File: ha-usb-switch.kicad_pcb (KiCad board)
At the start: 2 copper layers, 30 x 55 mm, 9 parts, among them J1 USB4125-GF-A-0190_REVA2, J4 USB1046-XX-XXXX-X-B-X_REVB, Q2 AO3401A, Q3 AO3400A, SW2 SW_SPDT, U1 MOUDLE-SEEEDUINO-XIAO-ESP32C3

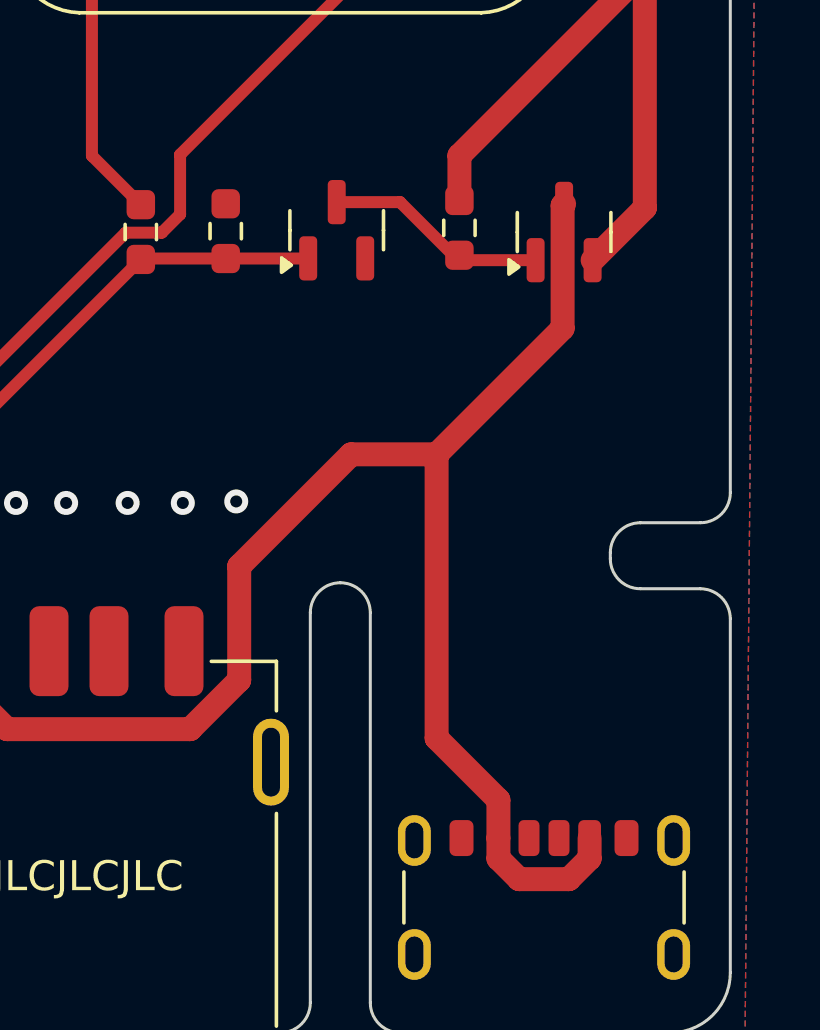
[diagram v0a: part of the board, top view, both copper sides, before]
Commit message: Add USB C sink pullups
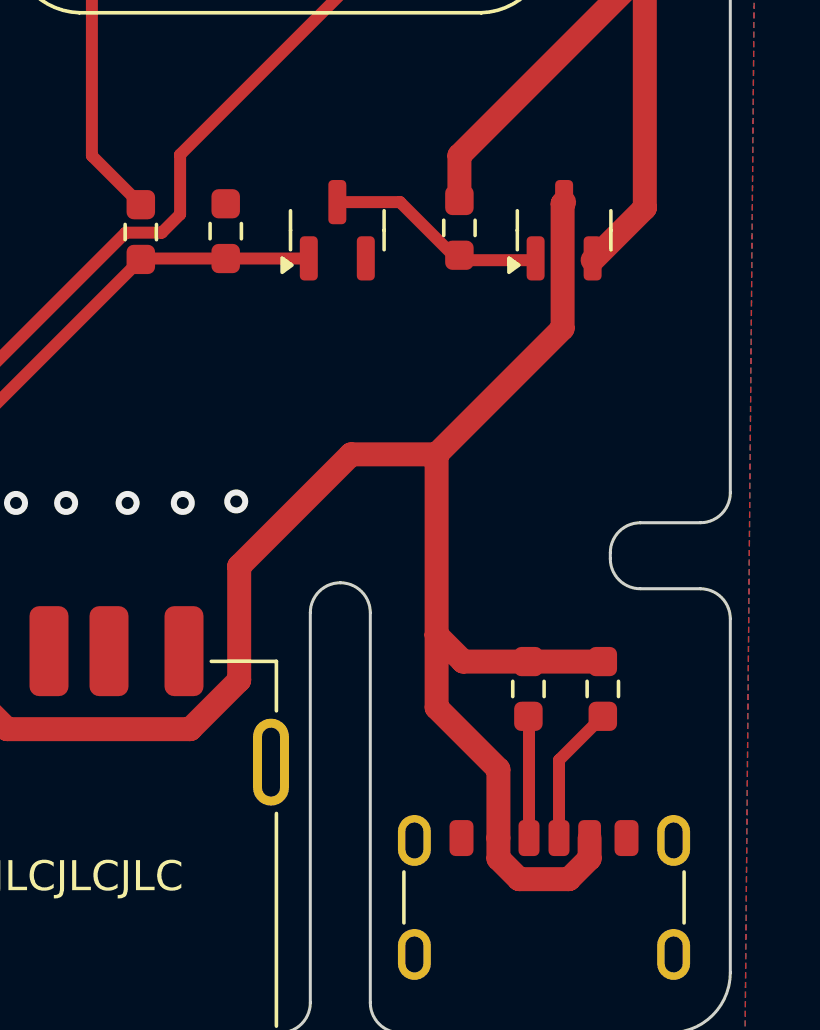
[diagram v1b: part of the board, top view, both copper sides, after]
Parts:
- added R4: 56k, Resistor_SMD:R_0603_1608Metric_Pad0.98x0.95mm_HandSolder, F.Cu at (43.3, 63.5)
- added R5: 56k, Resistor_SMD:R_0603_1608Metric_Pad0.98x0.95mm_HandSolder, F.Cu at (45.8, 63.5)
- moved Q2 0.06 mm to (44.5, 48.2)
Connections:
- J1 pad A5: unconnected-(J1-CC1-PadA5) -> Net-(J1-CC1)
- J1 pad B5: unconnected-(J1-CC2-PadB5) -> Net-(J1-CC2)
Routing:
- net +5V: track 52.1 -> 58.1 mm
- net Net-(J1-CC2): track 0.00 -> 4.66 mm
- net Net-(J1-CC1): track 0.00 -> 4.07 mm
